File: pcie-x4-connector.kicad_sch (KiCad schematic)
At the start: 2 parts, among them J7 Bus_M.2_1-2199230-6

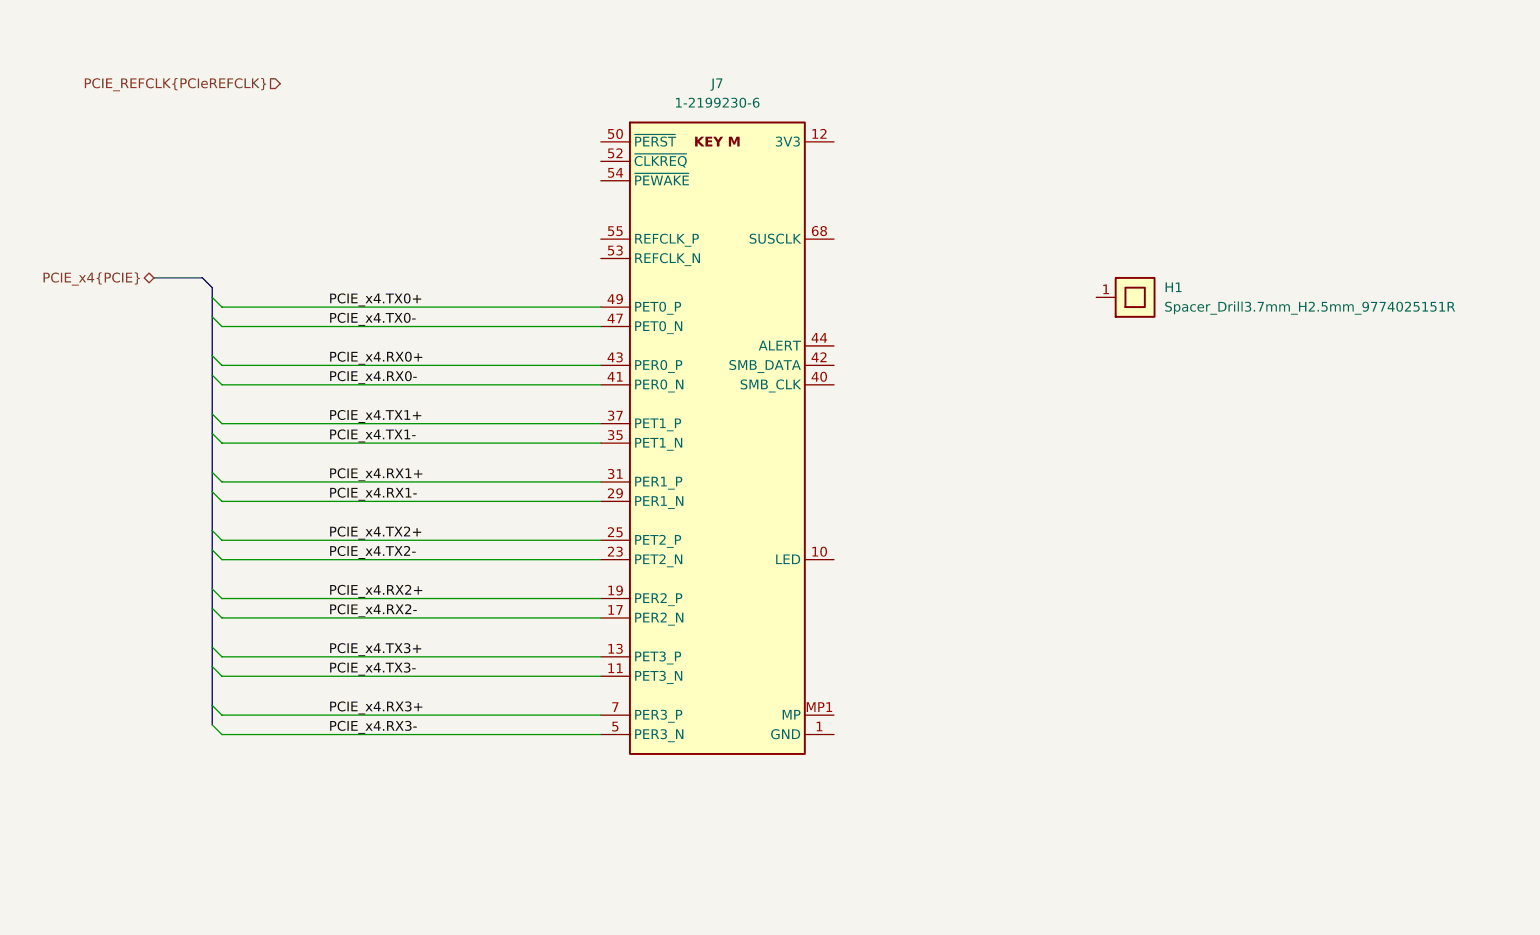
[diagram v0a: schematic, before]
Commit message: [#83338] Low speed PCIe x4 connections
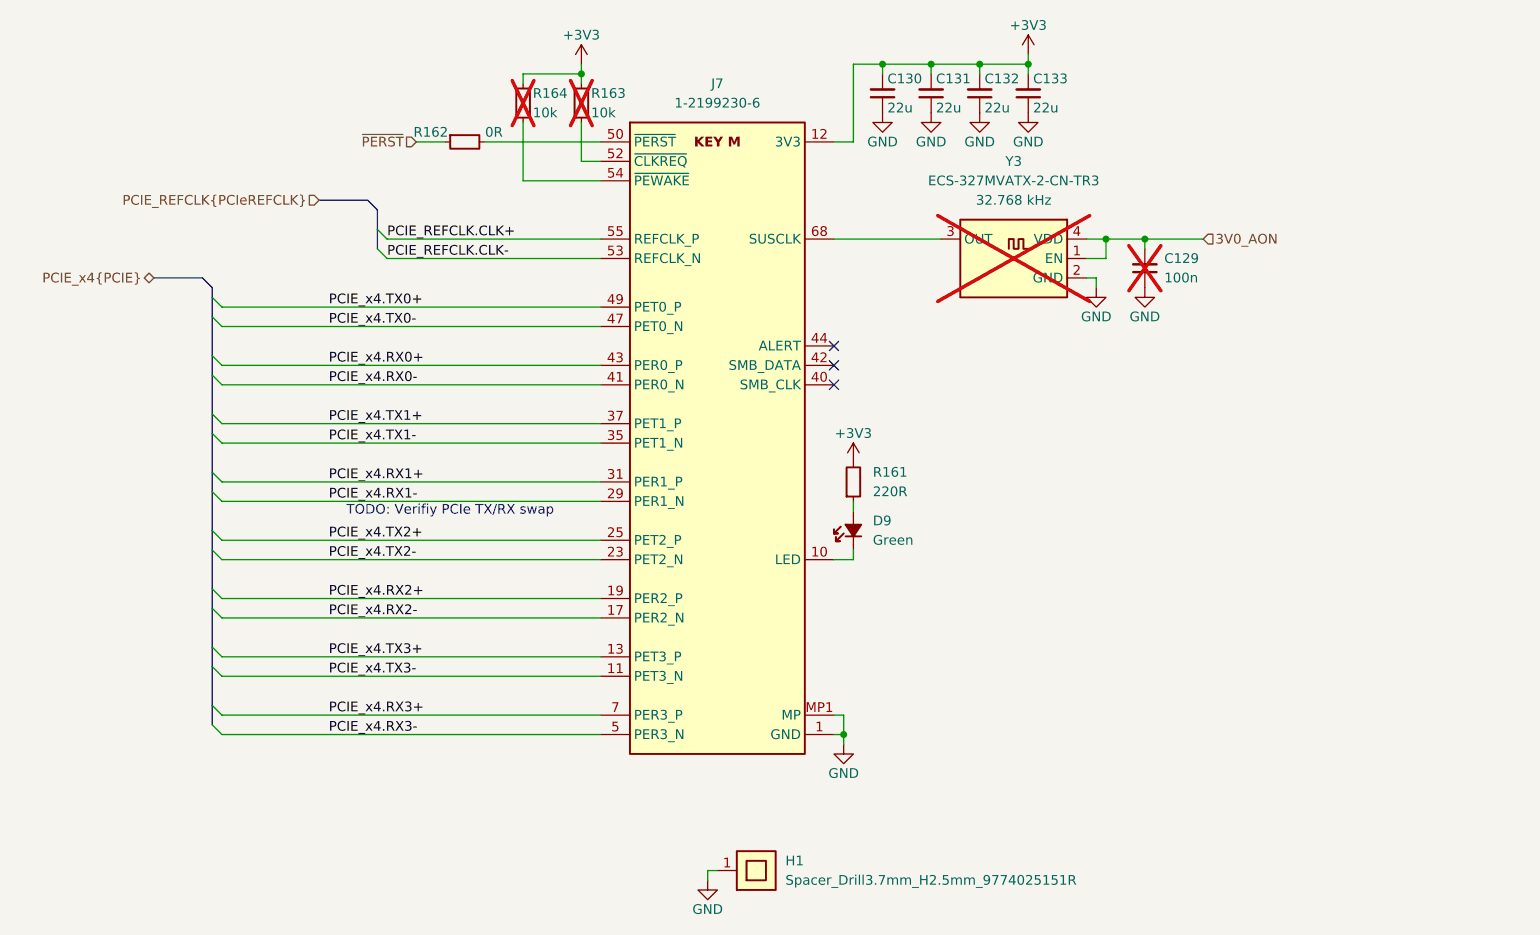
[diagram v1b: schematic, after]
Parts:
- added C129: C_100n_0402, antmicro-footprints:C_0402_1005Metric, symbol antmicroCapacitors0402:C_100n_0402
- added C130, C131, C132, C133: C_22u_0603, antmicro-footprints:C_0603_1608Metric, symbol antmicroCapacitors0603:C_22u_0603
- added D9: LED_G_0603_LTST-C190KGKT, antmicro-footprints:LED_0603_1608Metric_G, symbol antmicroLEDIndicationDiscrete:LED_G_0603_LTST-C190KGKT
- added R161: R_220R_0402, antmicro-footprints:R_0402_1005Metric, symbol antmicroResistors0402:R_220R_0402
- added R162: R_0R_0402, antmicro-footprints:R_0402_1005Metric, symbol antmicroResistors0402:R_0R_0402
- added R163, R164: R_10k_0402, antmicro-footprints:R_0402_1005Metric, symbol antmicroResistors0402:R_10k_0402
- added Y3: Oscillator_32.768kHz_ECS_2520MV, antmicro-footprints:Oscillator_SMD_ECS_2520MV_2.5x2mm, symbol antmicroOscillators:Oscillator_32.768kHz_ECS_2520MV
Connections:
- net GND: now reaches H1.1
- net GND: now also J7.1 (GND), J7.15 (GND), J7.21 (GND), J7.27 (GND), J7.3 (GND), J7.33 (GND), J7.39 (GND), J7.45 (GND), J7.51 (GND), J7.57 (GND), J7.71 (GND), J7.73 (GND), J7.75 (GND), J7.9 (GND), J7.MP1 (MP), J7.MP2 (MP), C129.1, C130.1, C131.1, C132.1, C133.1, Y3.2 (GND)
- net at J7.10 (LED): now also D9.1 (C)
- net +3V3: now reaches J7.12 (3V3), J7.14 (3V3), J7.16 (3V3), J7.18 (3V3), J7.2 (3V3), J7.4 (3V3), J7.70 (3V3), J7.72 (3V3), J7.74 (3V3)
- net +3V3: now also C130.2, C131.2, C132.2, C133.2, R161.2, R163.2, R164.2
- net at J7.50 (~{PERST}): now also R162.2
- net at J7.52 (~{CLKREQ}): now also R163.1
- net PCIE_REFCLK.CLK-: now reaches J7.53 (REFCLK_N)
- net at J7.54 (~{PEWAKE}): now also R164.1
- net PCIE_REFCLK.CLK+: now reaches J7.55 (REFCLK_P)
- net at J7.68 (SUSCLK): now also Y3.3 (OUT)
- new net: D9.2 (A), R161.1
- new net 3V0_AON: C129.2, Y3.1 (EN), Y3.4 (VDD)
- new net ~{PERST}: R162.1
- no-connect marks 0 -> 3
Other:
- note added: "TODO: Verifiy PCIe TX/RX swap"
- moved on the sheet: H1

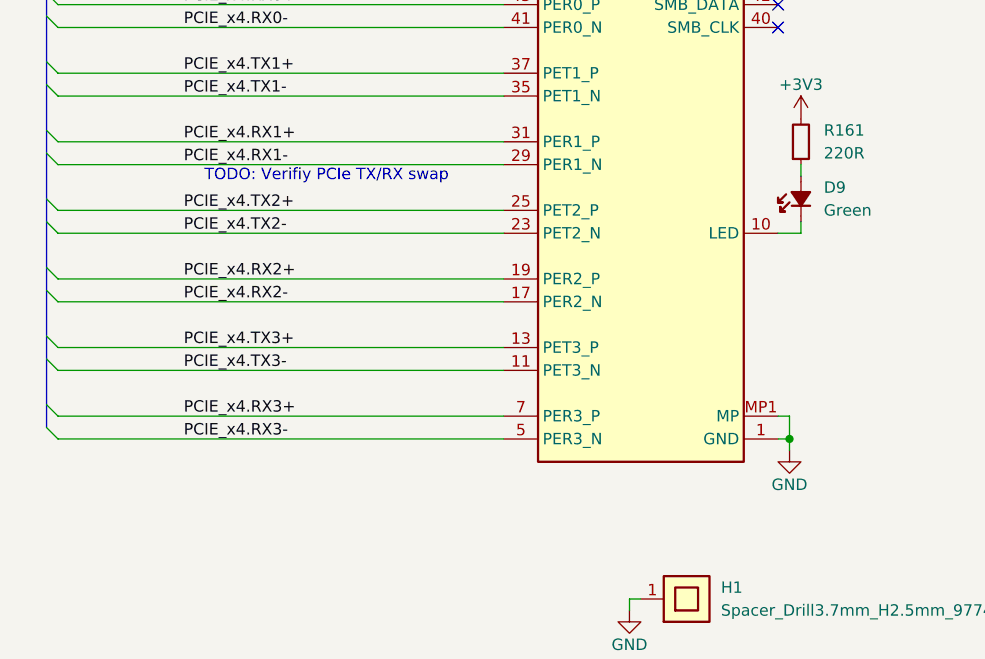
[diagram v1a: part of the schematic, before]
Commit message: [#83338] Fixed PCIe TX/RX
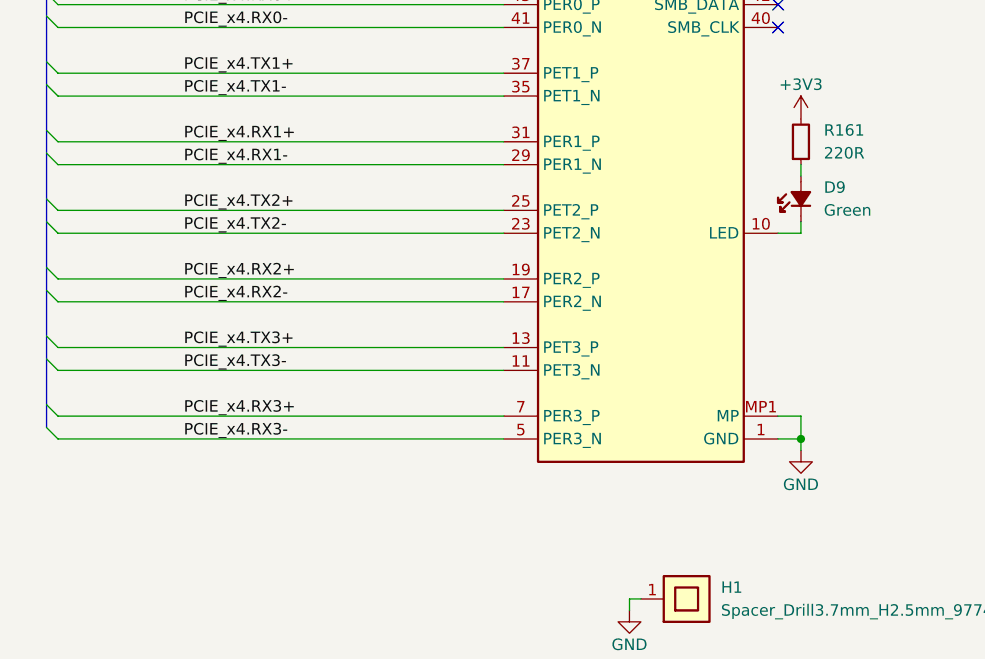
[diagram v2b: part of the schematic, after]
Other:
- note removed: "TODO: Verifiy PCIe TX/RX swap"
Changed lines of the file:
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@@
 		(rev "1.0.0")
 	)
-	(text "TODO: Verifiy PCIe TX/RX swap"
-		(exclude_from_sim no)
-		(at 173.355 147.32 0)
-		(effects
-			(font
-				(size 1.27 1.27)
-			)
-		)
-	)
 	(junction
 		(at 242.57 88.9)
@@
 	)
 	(junction
-		(at 224.79 176.53)
+		(at 226.06 176.53)
 		(diameter 0)
 		(color 0 0 0 0)
@@
 	(wire
 		(pts
-			(xy 224.79 173.99) (xy 224.79 176.53)
+			(xy 226.06 173.99) (xy 226.06 176.53)
 		)
 		(stroke
@@
 	(wire
 		(pts
-			(xy 224.79 176.53) (xy 224.79 177.8)
+			(xy 226.06 176.53) (xy 226.06 177.8)
 		)
 		(stroke
@@
 	(wire
 		(pts
-			(xy 223.52 176.53) (xy 224.79 176.53)
+			(xy 223.52 176.53) (xy 226.06 176.53)
 		)
 		(stroke
@@
 	(wire
 		(pts
-			(xy 223.52 173.99) (xy 224.79 173.99)
+			(xy 223.52 173.99) (xy 226.06 173.99)
 		)
 		(stroke
@@
 	(symbol
 		(lib_id "antmicropower:GND")
-		(at 224.79 177.8 0)
+		(at 226.06 177.8 0)
 		(unit 1)
 		(exclude_from_sim no)
@@
 		(dnp no)
 		(property "Reference" "#PWR0202"
-			(at 233.68 180.34 0)
+			(at 234.95 180.34 0)
 			(effects
 				(font
@@
 		)
 		(property "Value" "GND"
-			(at 224.79 181.61 0)
+			(at 226.06 181.61 0)
 			(effects
 				(font
@@
 		)
 		(property "Footprint" ""
-			(at 233.68 185.42 0)
+			(at 234.95 185.42 0)
 			(effects
 				(font
@@
 		)
 		(property "Datasheet" ""
-			(at 233.68 190.5 0)
+			(at 234.95 190.5 0)
 			(effects
 				(font
@@
 		)
 		(property "Description" ""
-			(at 224.79 177.8 0)
+			(at 226.06 177.8 0)
 			(effects
 				(font
@@
 		)
 		(property "Author" "Antmicro"
-			(at 233.68 185.42 0)
+			(at 234.95 185.42 0)
 			(effects
 				(font
@@
 		)
 		(property "License" "Apache-2.0"
-			(at 233.68 187.96 0)
+			(at 234.95 187.96 0)
 			(effects
 				(font

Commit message: [#83609] Reannotate board
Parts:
- renumbered C130 to C128, C131 to C129, C132 to C130, C133 to C131, C129 to C132, D9 to D12, H1 to H3, J7 to J10, R162 to R238, R164 to R239, R163 to R240, R161 to R241, Y3 to Y5
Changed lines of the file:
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@@
 		(dnp no)
 		(fields_autoplaced yes)
-		(property "Reference" "D9"
+		(property "Reference" "D12"
 			(at 228.6 148.59 90)
 			(effects
@@
 			(project ""
 				(path "/5f636c45-3c15-4731-8931-4625e0dab7e4/945730c0-5d04-4966-88eb-4ee840f8c440"
-					(reference "D9")
+					(reference "D12")
 					(unit 1)
 				)
@@
 		(on_board yes)
 		(dnp no)
-		(property "Reference" "R162"
+		(property "Reference" "R238"
 			(at 170.815 97.79 0)
 			(effects
@@
 			(project ""
 				(path "/5f636c45-3c15-4731-8931-4625e0dab7e4/945730c0-5d04-4966-88eb-4ee840f8c440"
-					(reference "R162")
+					(reference "R238")
 					(unit 1)
 				)
@@
 		(on_board yes)
 		(dnp no)
-		(property "Reference" "#PWR0384"
+		(property "Reference" "#PWR0246"
 			(at 257.81 97.79 0)
 			(effects
@@
 			(project "bmc-reference-carrier-board"
 				(path "/5f636c45-3c15-4731-8931-4625e0dab7e4/945730c0-5d04-4966-88eb-4ee840f8c440"
-					(reference "#PWR0384")
+					(reference "#PWR0246")
 					(unit 1)
 				)
@@
 		(on_board yes)
 		(dnp no)
-		(property "Reference" "C133"
+		(property "Reference" "C131"
 			(at 249.555 90.805 90)
 			(effects
@@
 			(project "bmc-reference-carrier-board"
 				(path "/5f636c45-3c15-4731-8931-4625e0dab7e4/945730c0-5d04-4966-88eb-4ee840f8c440"
-					(reference "C133")
+					(reference "C131")
 					(unit 1)
 				)
@@
 		(dnp yes)
 		(fields_autoplaced yes)
-		(property "Reference" "C129"
+		(property "Reference" "C132"
 			(at 266.7 114.2936 90)
 			(effects
@@
 			(project ""
 				(path "/5f636c45-3c15-4731-8931-4625e0dab7e4/945730c0-5d04-4966-88eb-4ee840f8c440"
-					(reference "C129")
+					(reference "C132")
 					(unit 1)
 				)
@@
 		(dnp no)
 		(fields_autoplaced yes)
-		(property "Reference" "H1"
+		(property "Reference" "H3"
 			(at 217.17 193.04 0)
 			(effects
@@
 			(project ""
 				(path "/5f636c45-3c15-4731-8931-4625e0dab7e4/945730c0-5d04-4966-88eb-4ee840f8c440"
-					(reference "H1")
+					(reference "H3")
 					(unit 1)
 				)
@@
 		(dnp yes)
 		(fields_autoplaced yes)
-		(property "Reference" "Y3"
+		(property "Reference" "Y5"
 			(at 247.015 101.6 0)
 			(effects
@@
 			(project ""
 				(path "/5f636c45-3c15-4731-8931-4625e0dab7e4/945730c0-5d04-4966-88eb-4ee840f8c440"
-					(reference "Y3")
+					(reference "Y5")
 					(unit 1)
 				)
@@
 		(on_board yes)
 		(dnp no)
-		(property "Reference" "C131"
+		(property "Reference" "C129"
 			(at 236.855 90.805 90)
 			(effects
@@
 			(project "bmc-reference-carrier-board"
 				(path "/5f636c45-3c15-4731-8931-4625e0dab7e4/945730c0-5d04-4966-88eb-4ee840f8c440"
-					(reference "C131")
+					(reference "C129")
 					(unit 1)
 				)
@@
 		(on_board yes)
 		(dnp no)
-		(property "Reference" "C130"
+		(property "Reference" "C128"
 			(at 230.505 90.805 90)
 			(effects
@@
 			(project ""
 				(path "/5f636c45-3c15-4731-8931-4625e0dab7e4/945730c0-5d04-4966-88eb-4ee840f8c440"
-					(reference "C130")
+					(reference "C128")
 					(unit 1)
 				)
@@
 		(on_board yes)
 		(dnp yes)
-		(property "Reference" "R163"
+		(property "Reference" "R240"
 			(at 191.77 92.71 90)
 			(effects
@@
 			(project ""
 				(path "/5f636c45-3c15-4731-8931-4625e0dab7e4/945730c0-5d04-4966-88eb-4ee840f8c440"
-					(reference "R163")
+					(reference "R240")
 					(unit 1)
 				)
@@
 		(on_board yes)
 		(dnp no)
-		(property "Reference" "#PWR0388"
+		(property "Reference" "#PWR0245"
 			(at 264.16 87.63 0)
 			(effects
@@
 			(project ""
 				(path "/5f636c45-3c15-4731-8931-4625e0dab7e4/945730c0-5d04-4966-88eb-4ee840f8c440"
-					(reference "#PWR0388")
+					(reference "#PWR0245")
 					(unit 1)
 				)
@@
 		(on_board yes)
 		(dnp no)
-		(property "Reference" "#PWR0380"
+		(property "Reference" "#PWR0238"
 			(at 205.74 88.9 0)
 			(effects
@@
 			(project ""
 				(path "/5f636c45-3c15-4731-8931-4625e0dab7e4/945730c0-5d04-4966-88eb-4ee840f8c440"
-					(reference "#PWR0380")
+					(reference "#PWR0238")
 					(unit 1)
 				)
@@
 		(on_board yes)
 		(dnp yes)
-		(property "Reference" "R164"
+		(property "Reference" "R239"
 			(at 184.15 92.71 90)
 			(effects
@@
 			(project "bmc-reference-carrier-board"
 				(path "/5f636c45-3c15-4731-8931-4625e0dab7e4/945730c0-5d04-4966-88eb-4ee840f8c440"
-					(reference "R164")
+					(reference "R239")
 					(unit 1)
 				)
@@
 		(dnp no)
 		(fields_autoplaced yes)
-		(property "Reference" "R161"
+		(property "Reference" "R241"
 			(at 228.6 142.24 90)
 			(effects
@@
 			(project ""
 				(path "/5f636c45-3c15-4731-8931-4625e0dab7e4/945730c0-5d04-4966-88eb-4ee840f8c440"
-					(reference "R161")
+					(reference "R241")
 					(unit 1)
 				)
@@
 		(on_board yes)
 		(dnp no)
-		(property "Reference" "#PWR0386"
+		(property "Reference" "#PWR0243"
 			(at 245.11 97.79 0)
 			(effects
@@
 			(project "bmc-reference-carrier-board"
 				(path "/5f636c45-3c15-4731-8931-4625e0dab7e4/945730c0-5d04-4966-88eb-4ee840f8c440"
-					(reference "#PWR0386")
+					(reference "#PWR0243")
 					(unit 1)
 				)
@@
 		(on_board yes)
 		(dnp no)
-		(property "Reference" "#PWR0202"
+		(property "Reference" "#PWR0241"
 			(at 234.95 180.34 0)
 			(effects
@@
 			(project ""
 				(path "/5f636c45-3c15-4731-8931-4625e0dab7e4/945730c0-5d04-4966-88eb-4ee840f8c440"
-					(reference "#PWR0202")
+					(reference "#PWR0241")
 					(unit 1)
 				)
@@
 		(on_board yes)
 		(dnp no)
-		(property "Reference" "C132"
+		(property "Reference" "C130"
 			(at 243.205 90.805 90)
 			(effects
@@
 			(project "bmc-reference-carrier-board"
 				(path "/5f636c45-3c15-4731-8931-4625e0dab7e4/945730c0-5d04-4966-88eb-4ee840f8c440"
-					(reference "C132")
+					(reference "C130")
 					(unit 1)
 				)
@@
 		(on_board yes)
 		(dnp no)
-		(property "Reference" "#PWR0387"
+		(property "Reference" "#PWR0242"
 			(at 238.76 97.79 0)
 			(effects
@@
 			(project ""
 				(path "/5f636c45-3c15-4731-8931-4625e0dab7e4/945730c0-5d04-4966-88eb-4ee840f8c440"
-					(reference "#PWR0387")
+					(reference "#PWR0242")
 					(unit 1)
 				)
@@
 		(on_board yes)
 		(dnp no)
-		(property "Reference" "#PWR0382"
+		(property "Reference" "#PWR0248"
 			(at 273.05 120.65 0)
 			(effects
@@
 			(project "bmc-reference-carrier-board"
 				(path "/5f636c45-3c15-4731-8931-4625e0dab7e4/945730c0-5d04-4966-88eb-4ee840f8c440"
-					(reference "#PWR0382")
+					(reference "#PWR0248")
 					(unit 1)
 				)
@@
 		(on_board yes)
 		(dnp no)
-		(property "Reference" "#PWR0385"
+		(property "Reference" "#PWR0244"
 			(at 251.46 97.79 0)
 			(effects
@@
 			(project "bmc-reference-carrier-board"
 				(path "/5f636c45-3c15-4731-8931-4625e0dab7e4/945730c0-5d04-4966-88eb-4ee840f8c440"
-					(reference "#PWR0385")
+					(reference "#PWR0244")
 					(unit 1)
 				)
@@
 		(on_board yes)
 		(dnp no)
-		(property "Reference" "#PWR0383"
+		(property "Reference" "#PWR0247"
 			(at 266.7 120.65 0)
 			(effects
@@
 			(project "bmc-reference-carrier-board"
 				(path "/5f636c45-3c15-4731-8931-4625e0dab7e4/945730c0-5d04-4966-88eb-4ee840f8c440"
-					(reference "#PWR0383")
+					(reference "#PWR0247")
 					(unit 1)
 				)
@@
 		(dnp no)
 		(fields_autoplaced yes)
-		(property "Reference" "J7"
+		(property "Reference" "J10"
 			(at 208.28 91.44 0)
 			(effects
@@
 			(project ""
 				(path "/5f636c45-3c15-4731-8931-4625e0dab7e4/945730c0-5d04-4966-88eb-4ee840f8c440"
-					(reference "J7")
+					(reference "J10")
 					(unit 1)
 				)
@@
 		(on_board yes)
 		(dnp no)
-		(property "Reference" "#PWR0381"
+		(property "Reference" "#PWR0239"
 			(at 215.9 198.12 0)
 			(effects
@@
 			(project "bmc-reference-carrier-board"
 				(path "/5f636c45-3c15-4731-8931-4625e0dab7e4/945730c0-5d04-4966-88eb-4ee840f8c440"
-					(reference "#PWR0381")
+					(reference "#PWR0239")
 					(unit 1)
 				)
@@
 		(on_board yes)
 		(dnp no)
-		(property "Reference" "#PWR0379"
+		(property "Reference" "#PWR0240"
 			(at 241.3 140.97 0)
 			(effects
@@
 			(project ""
 				(path "/5f636c45-3c15-4731-8931-4625e0dab7e4/945730c0-5d04-4966-88eb-4ee840f8c440"
-					(reference "#PWR0379")
+					(reference "#PWR0240")
 					(unit 1)
 				)
